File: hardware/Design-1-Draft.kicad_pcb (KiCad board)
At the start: 2 copper layers, 32 parts, among them J1 Barrel_Jack_Switch, M1 WATERPUMP-1, M2 WATERPUMP-2, Q1 IRLZ44N, Q2 IRLZ44N, SW1 Button, U3 ADS1115IDGS, U5 Tang_Nano_9K

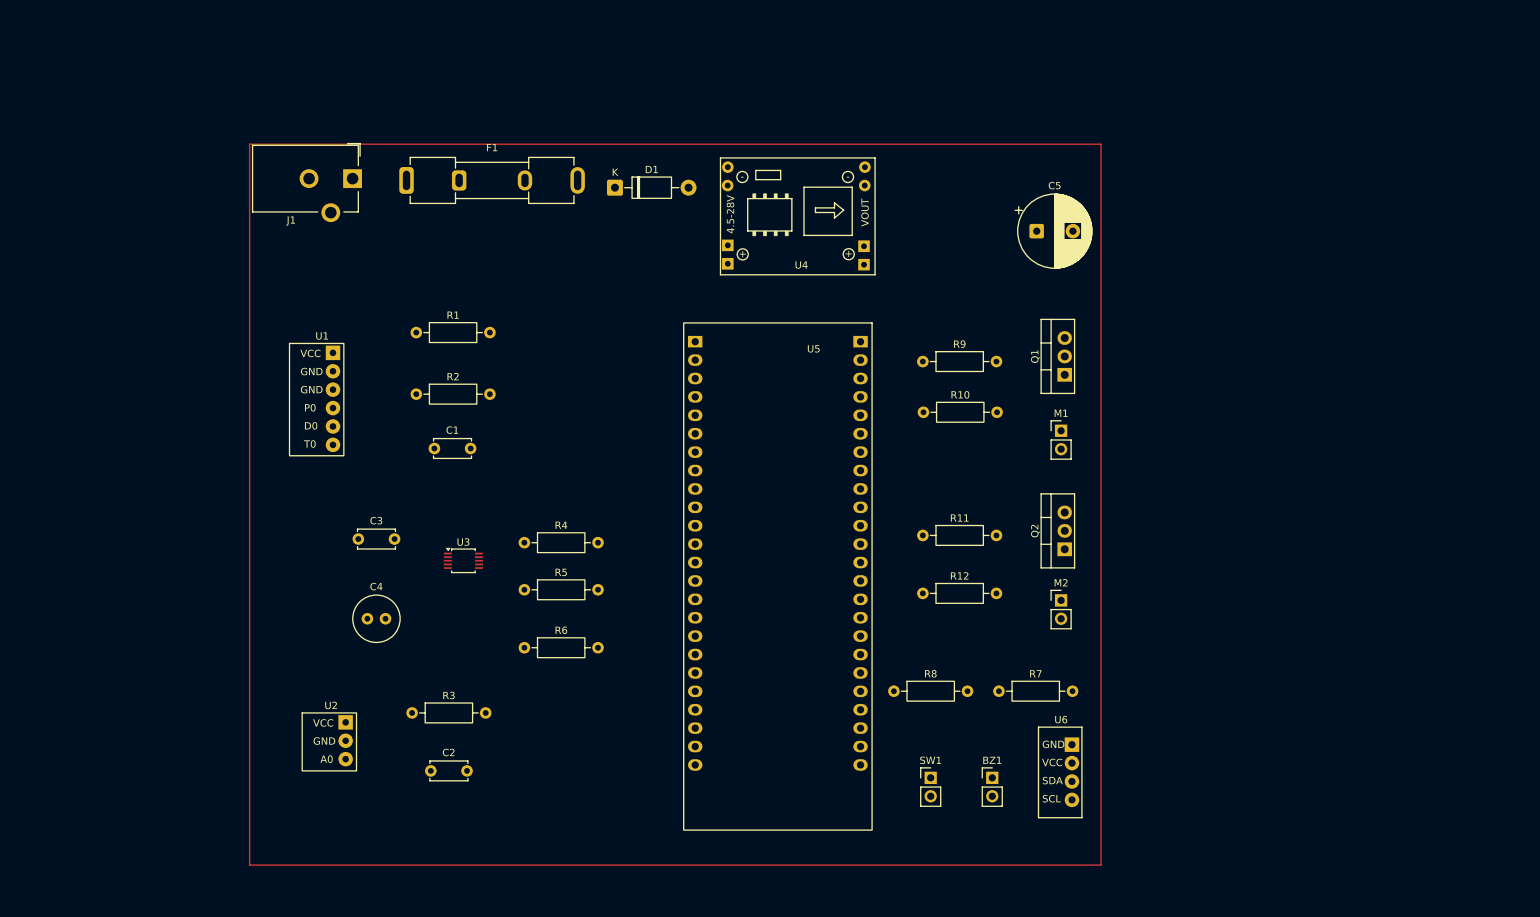
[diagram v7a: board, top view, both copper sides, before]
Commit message: realigned some footprints, figuring out trace paths
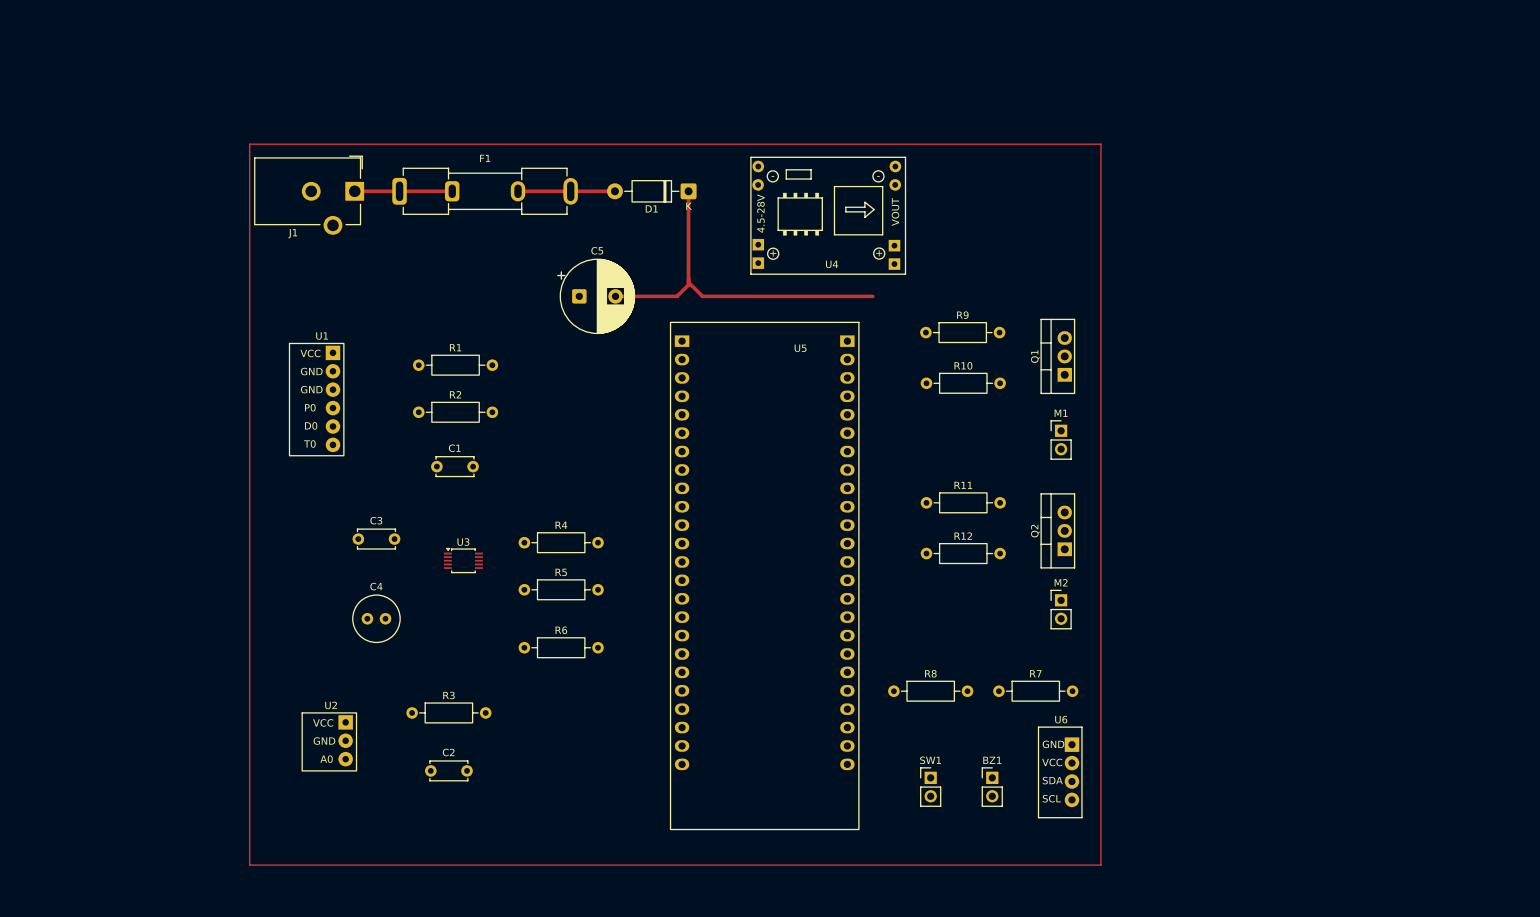
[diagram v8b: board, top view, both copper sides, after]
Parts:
- moved C5 63.8 mm to (112.0, 55.0)
- moved D1 10.2 mm to (127.1, 40.5), turned to 180 degrees
- moved R12 5.52 mm to (159.9, 90.5)
- moved R11 4.53 mm to (159.9, 83.5)
- moved R1 4.51 mm to (89.8, 64.5)
- moved U4 4.20 mm to (146.9, 43.3)
- moved R9 4.02 mm to (159.8, 60.0)
- moved R10 4.02 mm to (159.9, 67.0)
- moved C1 2.52 mm to (92.3, 78.5)
- moved R2 2.52 mm to (89.8, 71.0)
- moved U5 1.82 mm to (137.6, 90.4)
- moved F1 1.78 mm to (87.2, 40.5)
- moved J1 1.78 mm to (81.0, 40.5)
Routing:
- net Net-(D1-K): track 0.00 -> 50.4 mm
- net Net-(F1-Pad1): track 0.00 -> 13.5 mm
- net Net-(D1-A): track 0.00 -> 13.4 mm
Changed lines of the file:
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@@
 	(footprint "Connector_BarrelJack:BarrelJack_CUI_PJ-102AH_Horizontal"
 		(layer "F.Cu")
-		(at 80.7 38.75 -90)
+		(at 81 40.5 -90)
 		(descr "Thin-pin DC Barrel Jack, https://cdn-shop.adafruit.com/datasheets/21mmdcjackDatasheet.pdf")
 		(tags "Power Jack")
@@
 	(footprint "Resistor_THT:R_Axial_DIN0207_L6.3mm_D2.5mm_P10.16mm_Horizontal"
 		(layer "F.Cu")
-		(at 159.5 71)
+		(at 159.92 67)
 		(descr "Resistor, Axial_DIN0207 series, Axial, Horizontal, pin pitch=10.16mm, 0.25W = 1/4W, length*diameter=6.3*2.5mm^2, http://cdn-reichelt.de/documents/datenblatt/B400/1_4W%23YAG.pdf")
 		(tags "Resistor Axial_DIN0207 series Axial Horizontal pin pitch 10.16mm 0.25W = 1/4W length 6.3mm diameter 2.5mm")
@@
 	(footprint "Resistor_THT:R_Axial_DIN0207_L6.3mm_D2.5mm_P10.16mm_Horizontal"
 		(layer "F.Cu")
-		(at 159.42 64)
+		(at 159.84 60)
 		(descr "Resistor, Axial_DIN0207 series, Axial, Horizontal, pin pitch=10.16mm, 0.25W = 1/4W, length*diameter=6.3*2.5mm^2, http://cdn-reichelt.de/documents/datenblatt/B400/1_4W%23YAG.pdf")
 		(tags "Resistor Axial_DIN0207 series Axial Horizontal pin pitch 10.16mm 0.25W = 1/4W length 6.3mm diameter 2.5mm")
@@
 	(footprint "Resistor_THT:R_Axial_DIN0207_L6.3mm_D2.5mm_P10.16mm_Horizontal"
 		(layer "F.Cu")
-		(at 89.5 68.5)
+		(at 89.84 71)
 		(descr "Resistor, Axial_DIN0207 series, Axial, Horizontal, pin pitch=10.16mm, 0.25W = 1/4W, length*diameter=6.3*2.5mm^2, http://cdn-reichelt.de/documents/datenblatt/B400/1_4W%23YAG.pdf")
 		(tags "Resistor Axial_DIN0207 series Axial Horizontal pin pitch 10.16mm 0.25W = 1/4W length 6.3mm diameter 2.5mm")
@@
 	(footprint "Resistor_THT:R_Axial_DIN0207_L6.3mm_D2.5mm_P10.16mm_Horizontal"
 		(layer "F.Cu")
-		(at 159.42 88)
+		(at 159.92 83.5)
 		(descr "Resistor, Axial_DIN0207 series, Axial, Horizontal, pin pitch=10.16mm, 0.25W = 1/4W, length*diameter=6.3*2.5mm^2, http://cdn-reichelt.de/documents/datenblatt/B400/1_4W%23YAG.pdf")
 		(tags "Resistor Axial_DIN0207 series Axial Horizontal pin pitch 10.16mm 0.25W = 1/4W length 6.3mm diameter 2.5mm")
@@
 	(footprint "Resistor_THT:R_Axial_DIN0207_L6.3mm_D2.5mm_P10.16mm_Horizontal"
 		(layer "F.Cu")
-		(at 89.5 60)
+		(at 89.84 64.5)
 		(descr "Resistor, Axial_DIN0207 series, Axial, Horizontal, pin pitch=10.16mm, 0.25W = 1/4W, length*diameter=6.3*2.5mm^2, http://cdn-reichelt.de/documents/datenblatt/B400/1_4W%23YAG.pdf")
 		(tags "Resistor Axial_DIN0207 series Axial Horizontal pin pitch 10.16mm 0.25W = 1/4W length 6.3mm diameter 2.5mm")
@@
 	(footprint "Capacitor_THT:CP_Radial_D10.0mm_P5.00mm"
 		(layer "F.Cu")
-		(at 175.132323 46)
+		(at 112 55)
 		(descr "CP, Radial series, Radial, pin pitch=5.00mm, diameter=10mm, height=16mm, Electrolytic Capacitor")
 		(tags "CP Radial series Radial pin pitch 5.00mm diameter 10mm height 16mm Electrolytic Capacitor")
@@
 	(footprint "Fuse:Fuseholder_Clip-5x20mm_Keystone_3512P_Inline_P23.62x7.27mm_D1.02x2.41x1.02x1.57mm_Horizontal"
 		(layer "F.Cu")
-		(at 88.15 39)
+		(at 87.19 40.5)
 		(descr "Fuseholder Clips, 5x20mm Cylinder Fuse, Pins Inline, Horizontal, Keystone 3512P, http://www.keyelco.com/product-pdf.cfm?p=1386")
 		(tags "fuse clip open")
@@
 	(footprint "Diode_THT:D_DO-41_SOD81_P10.16mm_Horizontal"
 		(layer "F.Cu")
-		(at 116.92 40)
+		(at 127.08 40.5 180)
 		(descr "Diode, DO-41_SOD81 series, Axial, Horizontal, pin pitch=10.16mm, length*diameter=5.2*2.7mm^2, https://www.diodes.com/assets/Package-Files/DO-41-Plastic.pdf")
 		(tags "Diode DO-41_SOD81 series Axial Horizontal pin pitch 10.16mm  length 5.2mm diameter 2.7mm")
@@
 		(attr through_hole)
 		(fp_line
-			(start 1.34 0)
-			(end 2.36 0)
+			(start 8.82 0)
+			(end 7.8 0)
 			(stroke
 				(width 0.12)
@@
 		)
 		(fp_line
-			(start 3.14 -1.47)
-			(end 3.14 1.47)
+			(start 3.38 -1.47)
+			(end 3.38 1.47)
 			(stroke
 				(width 0.12)
@@
 		)
 		(fp_line
-			(start 3.38 -1.47)
-			(end 3.38 1.47)
+			(start 3.14 -1.47)
+			(end 3.14 1.47)
 			(stroke
 				(width 0.12)
@@
 		)
 		(fp_line
-			(start 8.82 0)
-			(end 7.8 0)
+			(start 1.34 0)
+			(end 2.36 0)
 			(stroke
 				(width 0.12)
@@
 		)
 		(fp_line
-			(start 0 0)
-			(end 2.48 0)
+			(start 10.16 0)
+			(end 7.68 0)
 			(stroke
 				(width 0.1)
@@
 		)
 		(fp_line
-			(start 3.16 -1.35)
-			(end 3.16 1.35)
+			(start 3.36 -1.35)
+			(end 3.36 1.35)
 			(stroke
 				(width 0.1)
@@
 		)
 		(fp_line
-			(start 3.36 -1.35)
-			(end 3.36 1.35)
+			(start 3.16 -1.35)
+			(end 3.16 1.35)
 			(stroke
 				(width 0.1)
@@
 		)
 		(fp_line
-			(start 10.16 0)
-			(end 7.68 0)
+			(start 0 0)
+			(end 2.48 0)
 			(stroke
 				(width 0.1)
@@
 		)
 		(pad "1" thru_hole roundrect
-			(at 0 0)
+			(at 0 0 180)
 			(size 2.2 2.2)
 			(drill 1.1)
@@
 		)
 		(pad "2" thru_hole circle
-			(at 10.16 0)
+			(at 10.16 0 180)
 			(size 2.2 2.2)
 			(drill 1.1)
@@
 	(footprint "1_CustomFootprints:SRT_MPT1584EN_Module"
 		(layer "F.Cu")
-		(at 142.66 43.388)
+		(at 146.864 43.301)
 		(tags "Power 5V 3A")
 		(property "Reference" "U4"
-			(at 0 7.3152 180)
+			(at 0 7.3152 0)
 			(layer "F.SilkS")
 			(effects
@@
 		)
 		(fp_text user "VOUT"
-			(at 8.8138 0.0508 270)
+			(at 8.8138 0.0508 90)
 			(layer "F.SilkS")
 			(effects
@@
 		)
 		(fp_text user "4.5-28V"
-			(at -9.7536 0.3048 270)
+			(at -9.7536 0.3048 90)
 			(layer "F.SilkS")
 			(effects
@@
 	(footprint "0my_project:DIP-48_TangNano9K"
 		(layer "F.Cu")
-		(at 139.40845 90.47 -90)
+		(at 137.59155 90.39 -90)
 		(property "Reference" "U5"
 			(at -28.194 -4.953 0)
@@
 	(footprint "Capacitor_THT:C_Disc_D5.0mm_W2.5mm_P5.00mm"
 		(layer "F.Cu")
-		(at 92 76)
+		(at 92.34 78.5)
 		(descr "C, Disc series, Radial, pin pitch=5.00mm, diameter*width=5*2.5mm^2, Capacitor, http://cdn-reichelt.de/documents/datenblatt/B300/DS_KERKO_TC.pdf")
 		(tags "C Disc series Radial pin pitch 5.00mm diameter 5mm width 2.5mm Capacitor")
@@
 	(footprint "Resistor_THT:R_Axial_DIN0207_L6.3mm_D2.5mm_P10.16mm_Horizontal"
 		(layer "F.Cu")
-		(at 159.42 96)
+		(at 159.92 90.5)
 		(descr "Resistor, Axial_DIN0207 series, Axial, Horizontal, pin pitch=10.16mm, 0.25W = 1/4W, length*diameter=6.3*2.5mm^2, http://cdn-reichelt.de/documents/datenblatt/B400/1_4W%23YAG.pdf")
 		(tags "Resistor Axial_DIN0207 series Axial Horizontal pin pitch 10.16mm 0.25W = 1/4W length 6.3mm diameter 2.5mm")
@@
 		(layer "F.Cu")
 	)
+	(segment
+		(start 127.08 53.08)
+		(end 129 55)
+		(width 0.5)
+		(layer "F.Cu")
+		(net 5)
+	)
+	(segment
+		(start 125.5 55)
+		(end 117 55)
+		(width 0.5)
+		(layer "F.Cu")
+		(net 5)
+	)
+	(segment
+		(start 129 55)
+		(end 152.5 55)
+		(width 0.5)
+		(layer "F.Cu")
+		(net 5)
+	)
+	(segment
+		(start 127.08 53.42)
+		(end 125.5 55)
+		(width 0.5)
+		(layer "F.Cu")
+		(net 5)
+	)
+	(segment
+		(start 127.08 52.5)
+		(end 127.08 53.42)
+		(width 0.5)
+		(layer "F.Cu")
+		(net 5)
+	)
+	(segment
+		(start 178.46 97)
+		(end 178.5 96.96)
+		(width 0.5)
+		(layer "F.Cu")
+		(net 5)
+	)
+	(segment
+		(start 127.08 40.5)
+		(end 127.08 53)
+		(width 0.5)
+		(layer "F.Cu")
+		(net 5)
+	)
+	(segment
+		(start 110.81 40.5)
+		(end 116.92 40.5)
+		(width 0.5)
+		(layer "F.Cu")
+		(net 6)
+	)
+	(segment
+		(start 103.54 40.5)
+		(end 110.81 40.5)
+		(width 0.5)
+		(layer "F.Cu")
+		(net 6)
+	)
+	(segment
+		(start 87.19 40.5)
+		(end 94.46 40.5)
+		(width 0.5)
+		(layer "F.Cu")
+		(net 64)
+	)
+	(segment
+		(start 81 40.5)
+		(end 87.19 40.5)
+		(width 0.5)
+		(layer "F.Cu")
+		(net 64)
+	)
 	(embedded_fonts no)
